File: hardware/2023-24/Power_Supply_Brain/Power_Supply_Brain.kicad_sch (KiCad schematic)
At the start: 69 parts, among them J1 Conn_02x03_Odd_Even, J2 Conn_01x02, J2 Conn_02x02_Counter_Clockwise, J3 USB_B_Micro, J5 Screw_Terminal_01x06, J6 Conn_02x11_Counter_Clockwise, SW1 SW_MEC_5G, U1 MAX17502G, U2 W25Q128JVS, U3 NCP1117-3.3_SOT223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

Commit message: design updated post review
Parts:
- removed C17 (x2): 10u, Capacitor_SMD:C_0805_2012Metric, symbol Device:C
- removed C17: 24n, Capacitor_SMD:C_0805_2012Metric, symbol Device:C
- removed R29: 120, Resistor_SMD:R_0603_1608Metric, symbol Device:R_Small_US
- removed R30: 3.12k, Resistor_SMD:R_0603_1608Metric, symbol Device:R_Small_US
- removed U3: NCP1117-3.3_SOT223, Package_TO_SOT_SMD:SOT-223-3_TabPin2, symbol Regulator_Linear:NCP1117-3.3_SOT223
- removed U5: NCP1117-ADJ_SOT223, Package_TO_SOT_SMD:SOT-223-3_TabPin2, symbol Regulator_Linear:NCP1117-ADJ_SOT223
- added C17: 22u, Capacitor_SMD:C_0805_2012Metric, symbol Device:C
- added C17: 22p, Capacitor_SMD:C_0402_1005Metric, symbol Device:C
- added C17: 12p, Capacitor_SMD:C_0402_1005Metric, symbol Device:C
- added C17: 10u, Capacitor_SMD:C_0805_2012Metric, symbol Device:C
- added C17: 100n, Capacitor_SMD:C_0402_1005Metric, symbol Device:C
- added C17: 2200p, Capacitor_SMD:C_0402_1005Metric, symbol Device:C
- added R21: 20k, Resistor_SMD:R_0402_1005Metric, symbol Device:R_Small_US
- added R32: 62k, Resistor_SMD:R_0402_1005Metric, symbol Device:R_Small_US
- added R33, R35: 30k, Resistor_SMD:R_0402_1005Metric, symbol Device:R_Small_US
- added R34: 135k, Resistor_SMD:R_0402_1005Metric, symbol Device:R_Small_US
- added U3: TPSM861252RDXR, TPSM861252:RDX0007A-MFG, symbol TPSM861252:TPSM861252RDXR
- added U5: NCP1117-5.0_SOT223, Package_TO_SOT_SMD:SOT-223-3_TabPin2, symbol Regulator_Linear:NCP1117-5.0_SOT223
- C12: value 2.2u -> 10u
- C16: value 910p -> 6800p
- C2, C3: value 27p -> 15p
- L1: value 39u -> 47u; MPN MSS1260-393MLD -> MSS1260-473ML
- R13: value 100k -> 174k; MPN ERA-3AEB104V -> (none)
- R16: value 11.1k -> 14k; MPN TNPW060311K1BEEA -> (none)
- R4, R5: value 27 -> 27.4
- Y1: MPN (none) -> ABM8-272-T3; Manufacturer (none) -> Abracon
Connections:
- net +3V3: now also C17.1, C17.1, R34.1, U3.3 (VOUT)
- net +9V: now also C17.1, C17.1, R32.1, U3.1 (VIN), U5.3 (VI)
- net ALRT_B1: now also U3.16 (GPIO13); no longer U3.15 (GPIO12)
- net ALRT_B2: now also U3.17 (GPIO14); no longer U3.16 (GPIO13)
- net ALRT_B3: now also U3.18 (GPIO15); no longer U3.17 (GPIO14)
- net EN_B1: now also U3.15 (GPIO12); no longer U3.14 (GPIO11)
- net EN_B2: now also U3.13 (GPIO10); no longer U3.12 (GPIO9)
- net EN_B3: now also U3.11 (GPIO8); no longer U3.9 (GPIO7)
- net GND: now also C17.2, C17.2, C17.2, C17.2, C17.2, R33.2, R35.2, U3.4 (PGND), U5.1 (GND)
- net PGD_B1: now also U3.14 (GPIO11); no longer U3.13 (GPIO10)
- net PGD_B2: now also U3.12 (GPIO9); no longer U3.11 (GPIO8)
- net PGD_B3: now also U3.9 (GPIO7); no longer U3.8 (GPIO6)
- net at U1.7 (NC/COMP): now also C17.1, R21.1
- net +5.5V renamed +5V
- net +5V: now also U5.2 (VO)
- net +9V_LX renamed +12V_LX
- new net: C17.1, R21.2
- new net: C17.2, R34.2, R35.1, U3.7 (FB)
- new net: R32.2, R33.1, U3.6 (EN)
- new net LED_EN: U3.8 (GPIO6)
- no-connect marks 2 -> 7
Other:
- moved on the sheet: C12, C13, C14, C16, C17, C2, C3, C5, D1, D2, D3, D4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

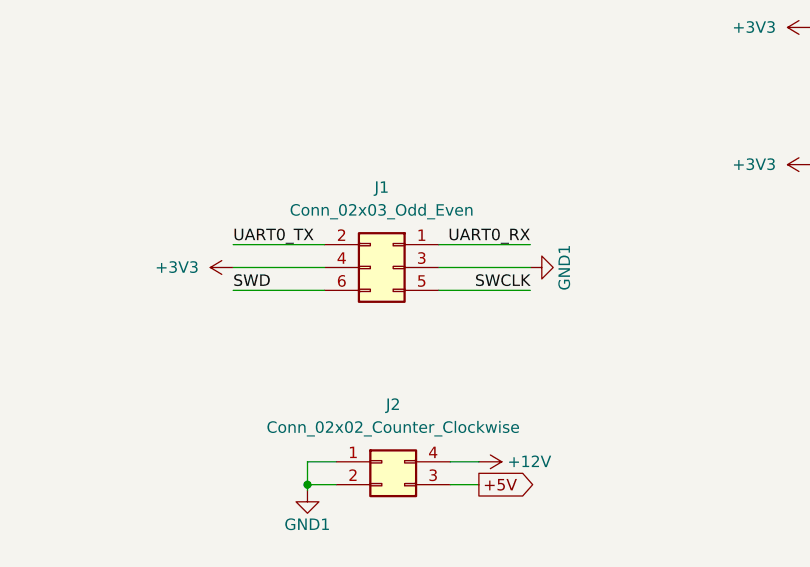
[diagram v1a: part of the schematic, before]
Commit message: Improved crystal layout. Re-ordered debug connector. Fixed silkscreen.
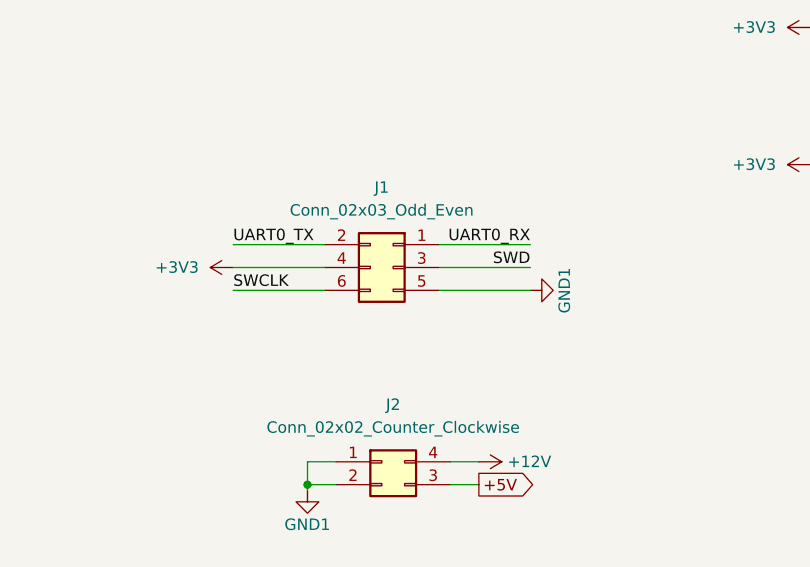
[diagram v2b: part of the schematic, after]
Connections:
- net GND: now also J1.5 (Pin_5); no longer J1.3 (Pin_3)
- net SWCLK: now also J1.6 (Pin_6); no longer J1.5 (Pin_5)
- net SWD: now also J1.3 (Pin_3); no longer J1.6 (Pin_6)

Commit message: Pushing for pre-production review
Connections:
- net GND: now also J6.11 (Pin_11)
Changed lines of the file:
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@@
+    (stroke (width 0) (type default))
+  )
+  (wire (pts (xy 356.87 157.48) (xy 356.87 158.75))
     (stroke (width 0) (type default))
   )
@@
   )
   (wire (pts (xy 69.215 136.525) (xy 78.105 136.525))
+    (stroke (width 0) (type default))
+  )
+  (wire (pts (xy 359.41 157.48) (xy 356.87 157.48))
     (stroke (width 0) (type default))
   )
@@
     )
   )
-  (global_label "ALRT_AUX3" (shape input) (at 374.65 160.02 0) (fields_autoplaced)
-    (effects (font (size 1.27 1.27)) (justify left))
-    (property "Intersheetrefs" "${INTERSHEET_REFS}" (at 387.7952 160.02 0)
+  (global_label "ALRT_AUX3" (shape input) (at 377.19 160.02 0) (fields_autoplaced)
+    (effects (font (size 1.27 1.27)) (justify left))
+    (property "Intersheetrefs" "${INTERSHEET_REFS}" (at 390.3352 160.02 0)
       (effects (font (size 1.27 1.27)) (justify left) hide)
     )
@@
     )
   )
-  (global_label "ALRT_AUX1" (shape input) (at 356.87 157.48 180) (fields_autoplaced)
-    (effects (font (size 1.27 1.27)) (justify right))
-    (property "Intersheetrefs" "${INTERSHEET_REFS}" (at 343.7248 157.48 0)
+  (global_label "ALRT_AUX1" (shape input) (at 354.33 157.48 180) (fields_autoplaced)
+    (effects (font (size 1.27 1.27)) (justify right))
+    (property "Intersheetrefs" "${INTERSHEET_REFS}" (at 341.1848 157.48 0)
       (effects (font (size 1.27 1.27)) (justify right) hide)
     )
@@
     )
   )
-  (global_label "ALRT_AUX2" (shape input) (at 356.87 160.02 180) (fields_autoplaced)
-    (effects (font (size 1.27 1.27)) (justify right))
-    (property "Intersheetrefs" "${INTERSHEET_REFS}" (at 343.7248 160.02 0)
+  (global_label "ALRT_AUX2" (shape input) (at 354.33 160.02 180) (fields_autoplaced)
+    (effects (font (size 1.27 1.27)) (justify right))
+    (property "Intersheetrefs" "${INTERSHEET_REFS}" (at 341.1848 160.02 0)
       (effects (font (size 1.27 1.27)) (justify right) hide)
     )
@@
         )
       )
+    )
+  )
+  (symbol (lib_id "power:GND1") (at 356.87 158.75 0) (unit 1)
+    (in_bom yes) (on_board yes) (dnp no)
+    (property "Reference" "#PWR063" (at 356.87 165.1 0)
+      (effects (font (size 1.27 1.27)) hide)
+    )
+    (property "Value" "GND1" (at 359.41 162.56 0)
+      (effects (font (size 1.27 1.27)) (justify right))
+    )
+    (property "Footprint" "" (at 356.87 158.75 0)
+      (effects (font (size 1.27 1.27)) hide)
+    )
+    (property "Datasheet" "" (at 356.87 158.75 0)
+      (effects (font (size 1.27 1.27)) hide)
+    )
+    (pin "1")
+    (instances
+      (project "Power_Supply_Brain"
+        (path "/3e3c1858-5f82-4870-a9c4-db8f7fe14a45"
+          (reference "#PWR063") (unit 1)
+        )
+      )
+      (project "2023-24_Power_Supply"
+        (path "/9d08c113-56e0-4c7c-90b4-94c67f8b2e1a"
+          (reference "#PWR033") (unit 1)
+        )
+      )
